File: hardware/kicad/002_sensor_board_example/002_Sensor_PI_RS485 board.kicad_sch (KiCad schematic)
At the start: 73 parts, among them J1 JST_SH, J2 JST_SH, J3 USB_C_Receptacle_USB2.0, U1 RP2354_60QFN, U4 TPD4E05U06DQAR, U5 THVD1424RGTR, U6 TPS62A0569ADRLR, Y1 ABM8-272-T3

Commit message: 002 sensor board: 5V bus rework, library consolidation, DRC pass
Board (002):
- Remove SS14 bridging diode; USB-C VBUS and JST V+ are now one net.
  Worst case is back-powering a host's VBUS, acceptable in a uniform
  5V fleet, and it drops 185mW in the bridging case.
- Remove the 8x 47k CS pull-ups. At 47k they parked the TLA2518 CS
  inputs mid-rail (1.7-2.1V, between VIL 0.99 and VIH 2.31); the
  internal pull-down now defines them cleanly low. Firmware must drive
  CS high before configuring SPI.
- 5V pour along the bottom edge, 3.3V moved up to the mounting rail.
- USB-C relocated; ~200mm D+/D- run on F.Cu over the B.Cu GND pour.
- Screw-head keepouts on all mounting holes.
- Board grown 2mm in Y -> 413.66 x 35.00 mm.

Net classes:
- USB_DIFF_90 -> USB_FS, diff pair 0.8/0.15 -> 0.35/0.15. The old name
  claimed 90 ohm; on a 1.51mm 2-layer stackup it is ~140 ohm and cannot
  be otherwise. Irrelevant at Full Speed.
- Add PWR_5V (+5V) and RS485 (/RS485_P, /RS485_N).
- Restore the +3V3 -> VCC assignment lost during the rename.

Libraries:
- footprints/ -> footprints.pretty/ so KiCad will save into it.
- Consolidate symbols into PHOTON / PHOTON_Modified on 001d and 002;
  drop unused vendor-exported libraries.
- Add mousebite_34mm: 17x 1.2mm NPTH at 2mm pitch. 0.8mm webs cut more
  easily than the old 1.4mm and still pass a 0.3mm trace.
- Fix MountingHole_2.7mm_M2.5_Keepout: it disallowed pads, so each hole
  flagged its own NPTH (17 DRC errors).

Fab outputs now tracked via .gitignore negation for production/*.csv.

Co-Authored-By: Claude Opus 5 <noreply@anthropic.com>
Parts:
- removed CR2: PTVSHC3D7VU, footprints:SOD-323_L1.8-W1.3-LS2.5-RD, symbol PTVSHC3D7VU:PTVSHC3D7VU
- removed D1: SS14, Diode_SMD:D_SMA, symbol Device:D_Schottky
- removed J4: (no value), Connector_PinHeader_1.27mm:PinHeader_1x04_P1.27mm_Vertical, symbol Connector_Generic:Conn_01x04
- added C22, C23, C24, C25, C26, C27: 100nF, Capacitor_SMD:C_0402_1005Metric, symbol Device:C
- added H17: MountingHole, footprints:MountingHole_2.7mm_M2.5_Keepout, symbol Mechanical:MountingHole
- CR1: symbol PTVSHC3D7VU:PTVSHC3D7VU -> PHOTON:PTVSHC3D7VU
- H1, H10, H11, H12, H13, H14, H15, H16, H2, H3, H4, H5, H6, H7, H8, H9: footprint MountingHole:MountingHole_2.7mm_M2.5 -> footprints:MountingHole_2.7mm_M2.5_Keepout
- J3: symbol Connector:USB_C_Receptacle_USB2.0 -> PHOTON_Modified:USB_C_Receptacle_USB2.0
- JP1, JP2: footprint (none) -> Jumper:SolderJumper-2_P1.3mm_Open_RoundedPad1.0x1.5mm; symbol Jumper:SolderJumper_2_Open -> PHOTON_Modified:SolderJumper_2_Open
- JP4: symbol Jumper:SolderJumper_2_Open -> PHOTON_Modified:SolderJumper_2_Open
- U1: symbol MCU_RaspberryPi_RP2350:RP2350_60QFN -> PHOTON:RP2350_60QFN
- U4: symbol 2025-08-11_08-44-22:TPD4E05U06QDQARQ1 -> PHOTON:TPD4E05U06QDQARQ1
- U5: symbol 2025-11-21_08-29-10_THVD1424RGTR:THVD1424RGTR -> PHOTON:THVD1424RGTR
- U6: footprint Pretty Custom:DRL0006A-MFG -> footprints:SOT-563_DRL0006A; symbol TI BUCK:TPS62A0569ADRLR -> PHOTON:TPS62A0569ADRLR
- Y1: symbol Device:Crystal_GND24 -> PHOTON_Modified:Crystal_GND24
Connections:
- net GND: now also C22.2, C23.2, C24.2, C25.2, C26.2, C27.2
- net VBUS renamed +5V
- net +5V: now also C22.1, C23.1, C24.1, C25.1, C26.1, C27.1
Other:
- note removed: "Debug Connector"
- moved on the sheet: CR1

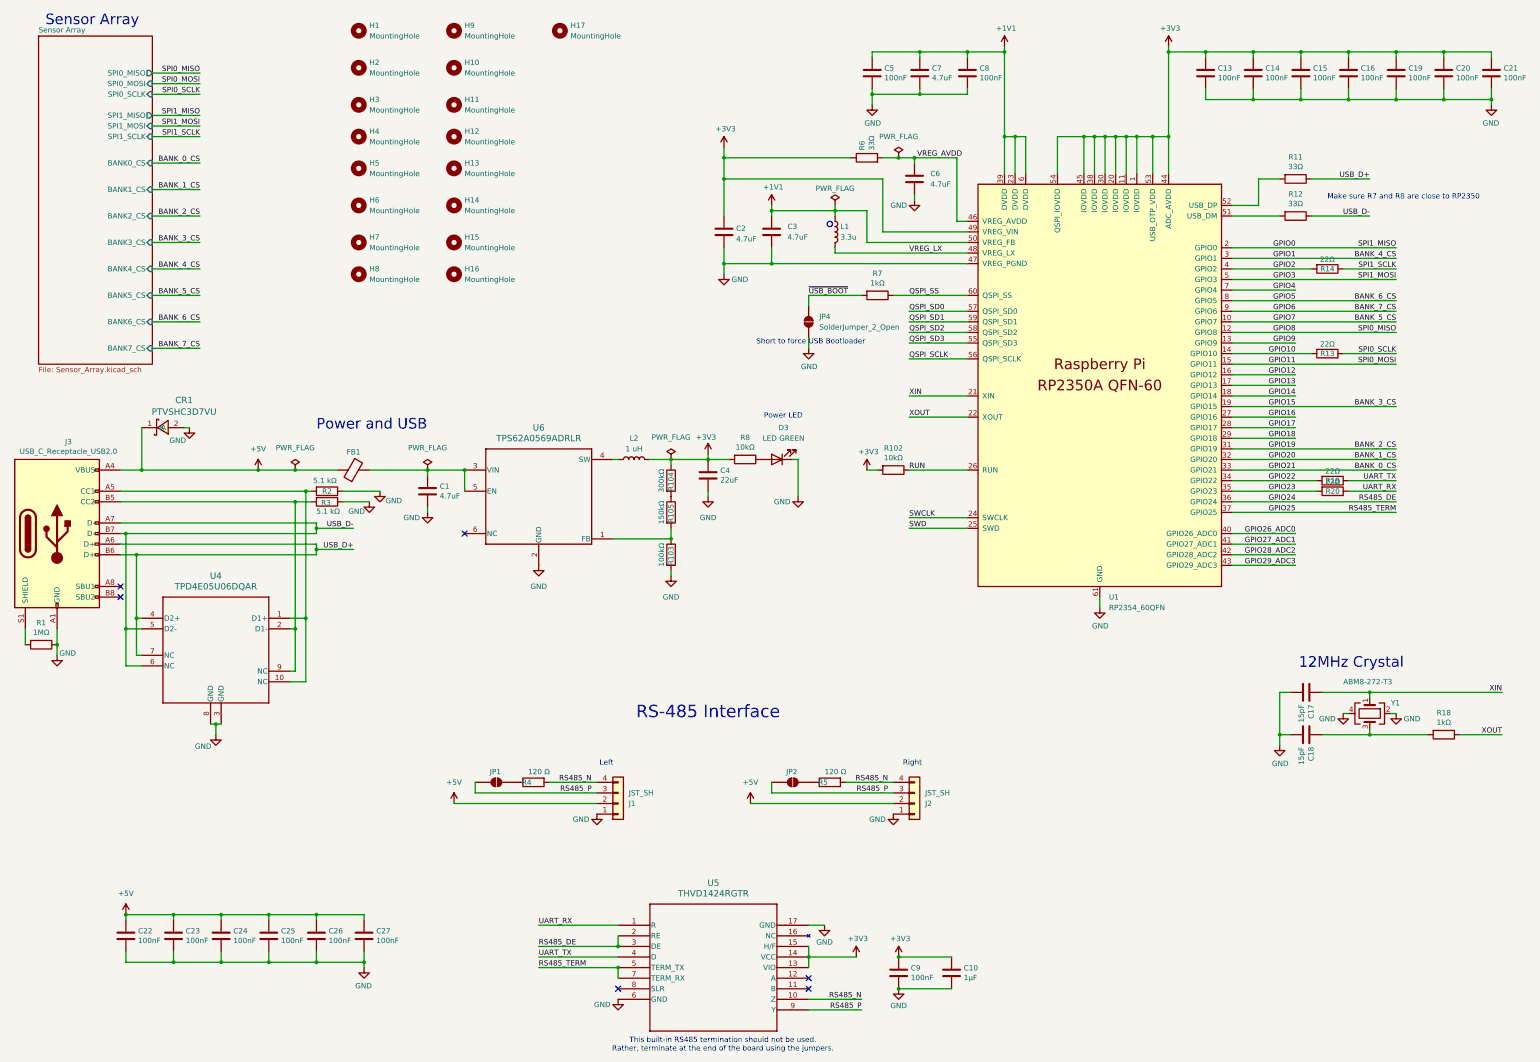
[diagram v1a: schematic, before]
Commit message: 002: ERC/DRC to zero, symbol and value cleanup
Schematic (ERC 24 -> 0):
- VCNT2020 renamed to VCNT2025X01, matching the part actually fitted.
  Pin types preserved: passive / open_collector / passive / passive.
  The old auto-generated VCNT2025X01 symbol (all pins Unspecified) is gone.
- THVD1424RGTR: 10 pins off Unspecified (R, RE, DE, D, TERM_TX, TERM_RX,
  Y, Z, VIO, H/F). VIO was typed as a signal despite being a supply pin.
- TLA2518IRTER: DECAP -> Passive, clearing 8 warnings at once.
- PWR_FLAG moved off J3's VBUS (which J3 already drives as a Power output)
  onto GND, which had none. One move, two errors.
- JP1/JP2/JP4 repointed to stock Jumper:SolderJumper_2_Open. The project
  copy was KiCad's older stock symbol, not a deliberate modification.
- R1 1M -> 0 ohm, bonding the USB-C shell to GND. A lone 1M is a static
  bleed, not a shield connection: open at every frequency that matters,
  and it isolated nothing since J3's GND pins are already bonded.

Layout:
- MountingHole keepout had (pads not_allowed), so each hole flagged its
  own NPTH. Fixed and patched into all 17 instances.
- Mousebite silkscreen removed (library + all 3 placements). The dashed
  line crossed the pours end to end and caused ~61 of the DRC warnings.
- 30 duplicate vias deleted. Each pair was 1 nm apart from a float->int
  round-trip in the layout plugin, so KiCad's "delete redundant vias"
  could not see them while DRC's co-located check could.
- min_resolved_spokes 2 -> 1; single-spoke pads are accepted on this
  board rather than excluded per-violation.

BOM hygiene:
- Component values normalised: no space before units, ASCII u instead of
  U+03BC, and 3.3u given its missing unit. Merges 100 kohm/100kohm and
  1 uF/1uF, which would otherwise export as separate lines for identical
  parts. 181 edits across schematics and PCB, kept in sync.

Libraries:
- PHOTON_Modified reduced to the two symbols that genuinely diverge from
  stock: Crystal_GND24 and USB_C_Receptacle_USB2.0.

Known o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
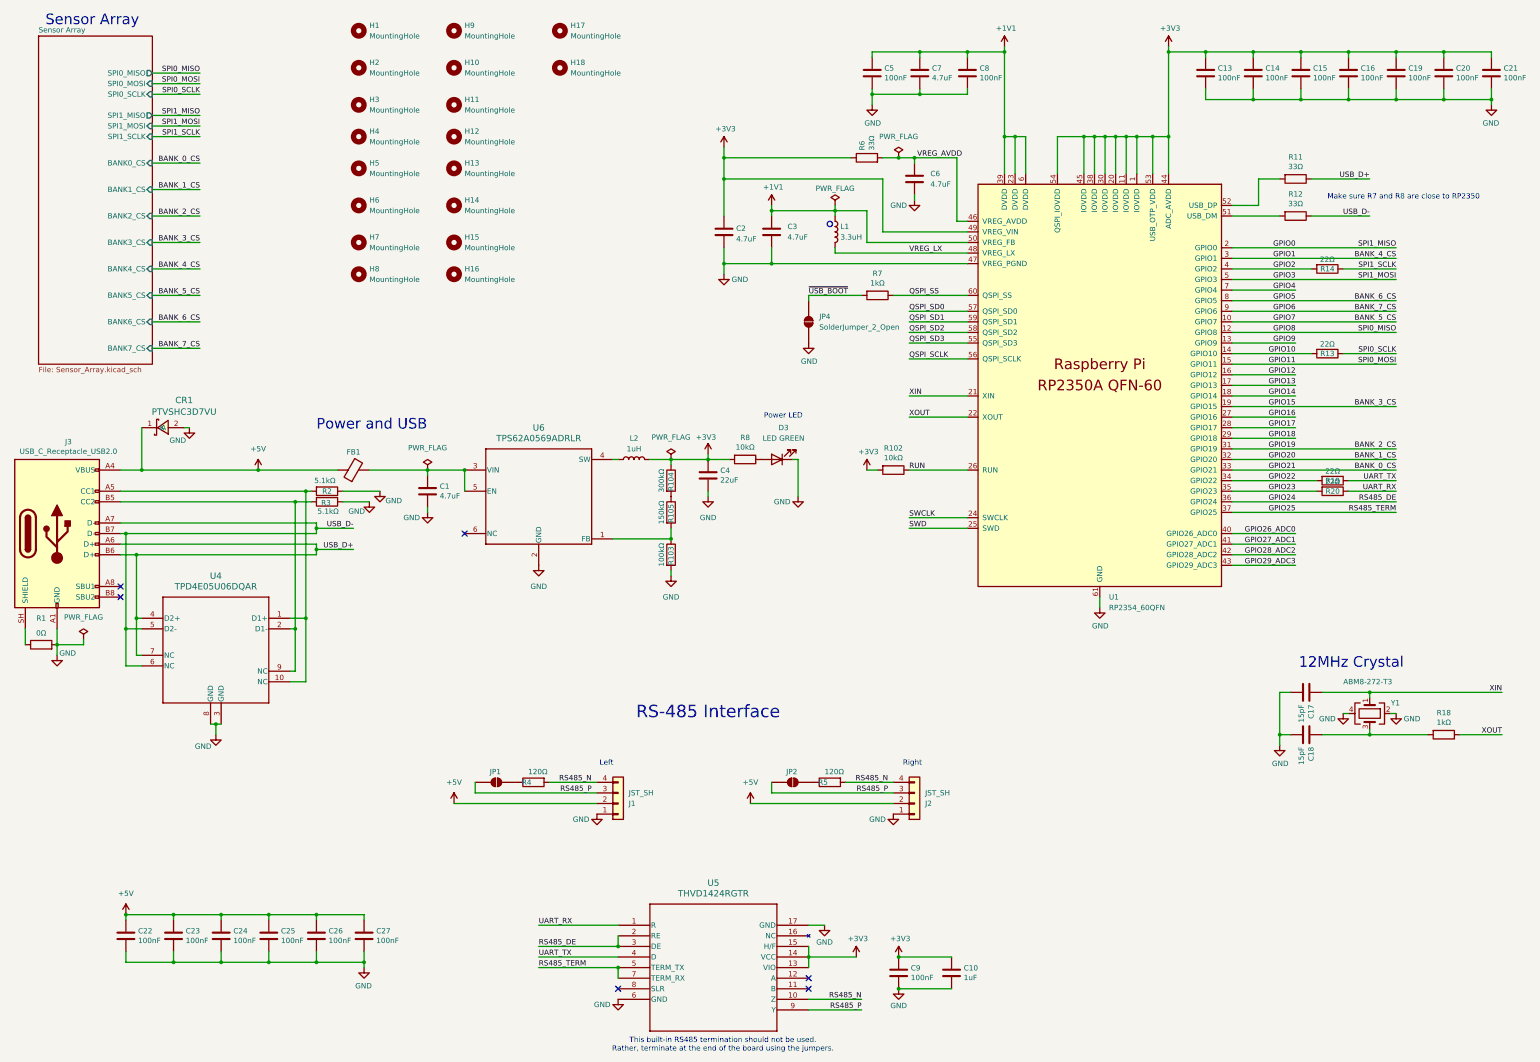
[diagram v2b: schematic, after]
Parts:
- added H18: MountingHole, footprints:MountingHole_2.7mm_M2.5_Keepout, symbol Mechanical:MountingHole
- C1: Part # CL21A475KAQNNNE -> (none)
- C10: value 1μF -> 1uF
- CR1: LCSC Part C110753 -> (none)
- JP1, JP2, JP4: symbol PHOTON_Modified:SolderJumper_2_Open -> Jumper:SolderJumper_2_Open
- L1: value 3.3u -> 3.3uH
- L2: value 1 uH -> 1uH
- R1: value 1MΩ -> 0Ω; footprint Resistor_SMD:R_0805_2012Metric_Pad1.20x1.40mm_HandSolder -> Resistor_SMD:R_0402_1005Metric
- R2, R3: value 5.1 kΩ -> 5.1kΩ
- R4, R5: value 120 Ω -> 120Ω
- U5: JLCPCB Part # (none) -> C5359161
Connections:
- net GND: now also R1.2; no longer R1.1
- new net: J3.SH (SHIELD), R1.1
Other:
- note removed: "Short to force USB Bootloader"
